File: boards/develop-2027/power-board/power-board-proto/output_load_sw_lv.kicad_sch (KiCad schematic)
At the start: 9 parts, among them Q2 T2N7002BK,LM, Q3 AOD4185

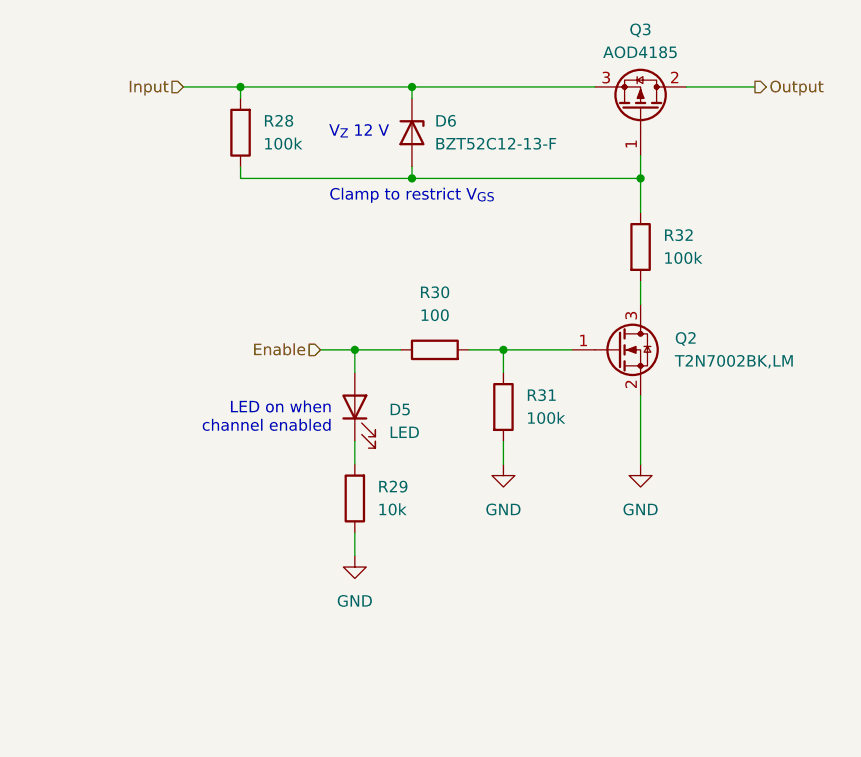
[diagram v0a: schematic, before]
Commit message: add fixes for problems caught by AI design review
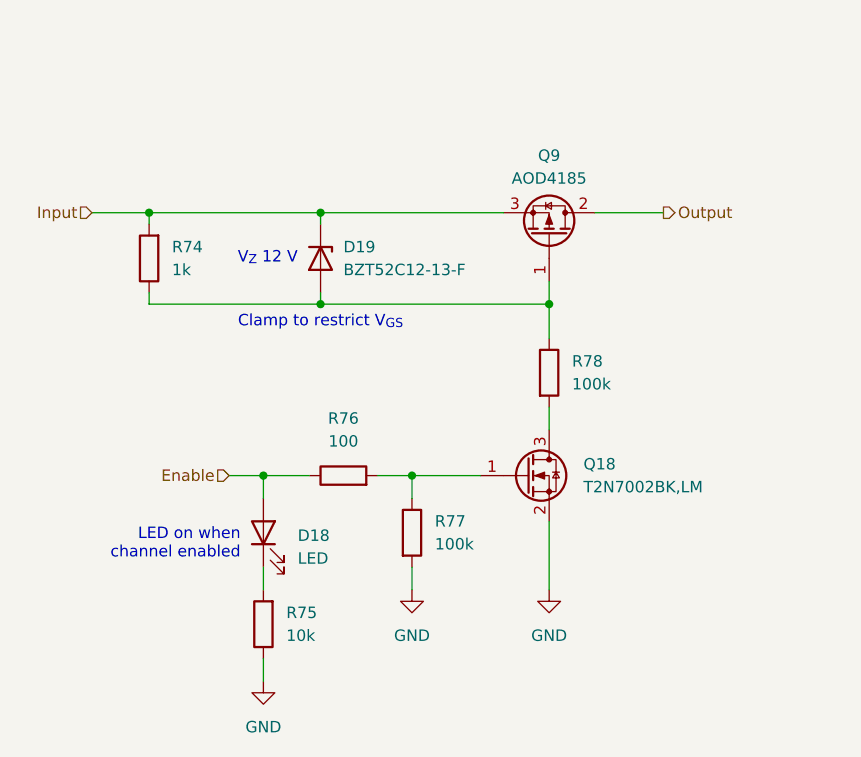
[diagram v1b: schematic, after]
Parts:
- removed D5: LED, LED_SMD:LED_0603_1608Metric_Pad1.05x0.95mm_HandSolder, symbol Device:LED
- removed D6: BZT52C12-13-F, Diode_SMD:D_SOD-123, symbol Device:D_Zener
- removed Q2: T2N7002BK,LM, Package_TO_SOT_SMD:SOT-23-3, symbol Transistor_FET:Q_NMOS_GSD
- removed Q3: AOD4185, Package_TO_SOT_SMD:TO-252-2, symbol Transistor_FET:Q_PMOS_GDS
- removed R28, R31, R32: 100k, Resistor_SMD:R_0603_1608Metric_Pad0.98x0.95mm_HandSolder, symbol Device:R
- removed R29: 10k, Resistor_SMD:R_0603_1608Metric_Pad0.98x0.95mm_HandSolder, symbol Device:R
- removed R30: 100, Resistor_SMD:R_0603_1608Metric_Pad0.98x0.95mm_HandSolder, symbol Device:R
- added D18: LED, LED_SMD:LED_0603_1608Metric_Pad1.05x0.95mm_HandSolder, symbol Device:LED
- added D19: BZT52C12-13-F, Diode_SMD:D_SOD-123, symbol Device:D_Zener
- added Q18: T2N7002BK,LM, Package_TO_SOT_SMD:SOT-23-3, symbol Transistor_FET:Q_NMOS_GSD
- added Q9: AOD4185, Package_TO_SOT_SMD:TO-252-2, symbol Transistor_FET:Q_PMOS_GDS
- added R74: 1k, Resistor_SMD:R_0603_1608Metric_Pad0.98x0.95mm_HandSolder, symbol Device:R
- added R75: 10k, Resistor_SMD:R_0603_1608Metric_Pad0.98x0.95mm_HandSolder, symbol Device:R
- added R76: 100, Resistor_SMD:R_0603_1608Metric_Pad0.98x0.95mm_HandSolder, symbol Device:R
- added R77, R78: 100k, Resistor_SMD:R_0603_1608Metric_Pad0.98x0.95mm_HandSolder, symbol Device:R
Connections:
- net Enable: now also D18.2 (A), R76.1
- net GND: now also Q18.2 (S), R75.1, R77.2
- net Input: now also D19.1 (K), Q9.3 (S), R74.2
- net Output: now also Q9.2 (D)
- new net: Q18.1 (G), R76.2, R77.1
- new net: Q18.3 (D), R78.2
- new net: D18.1 (K), R75.2
- new net: D19.2 (A), Q9.1 (G), R74.1, R78.1
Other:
- title: 40 V, 40 A Output Load Switch -> (none)

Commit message: finalize DigiKey part numbers
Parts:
- D18: Manufacturer P/N (none) -> LTST-C190KRKT; Vendor (none) -> DigiKey; Vendor P/N (none) -> 160-1436-1-ND
- R74: Manufacturer P/N (none) -> RC0603FR-071KL; Vendor (none) -> DigiKey; Vendor P/N (none) -> 311-1.00KHRCT-ND
- R75: Manufacturer P/N (none) -> RC0603FR-0710KL; Vendor (none) -> DigiKey; Vendor P/N (none) -> 311-10.0KHRCT-ND
- R76: Manufacturer P/N (none) -> CRCW0603100RFKEA; Vendor (none) -> DigiKey; Vendor P/N (none) -> 541-100HCT-ND
- R77, R78: Manufacturer P/N (none) -> RC0603FR-07100KL; Vendor (none) -> DigiKey; Vendor P/N (none) -> 311-100KHRCT-ND
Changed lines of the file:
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@@
 			)
 		)
-		(property "Datasheet" ""
+		(property "Datasheet" "https://yageogroup.com/content/datasheet/asset/file/PYU-RC_GROUP_51_ROHS_L"
 			(at 120.65 134.62 0)
 			(hide yes)
@@
 			)
 		)
-		(property "Description" "Resistor"
+		(property "Description" "10 kOhms ±1% 0.1W, 1/10W Chip Resistor 0603 (1608 Metric) Moisture Resistant Thick Film"
 			(at 120.65 134.62 0)
 			(hide yes)
@@
 			)
 		)
-		(property "Manufacturer P/N" ""
+		(property "Manufacturer P/N" "RC0603FR-0710KL"
 			(at 120.65 134.62 0)
 			(hide yes)
@@
 			)
 		)
-		(property "Vendor" ""
+		(property "Vendor" "DigiKey"
 			(at 120.65 134.62 0)
 			(hide yes)
@@
 			)
 		)
-		(property "Vendor P/N" ""
+		(property "Vendor P/N" "311-10.0KHRCT-ND"
 			(at 120.65 134.62 0)
 			(hide yes)
@@
 			)
 		)
-		(property "Datasheet" ""
+		(property "Datasheet" "https://optoelectronics.liteon.com/upload/download/DS-22-99-0151/LTST-C190KRKT.pdf"
 			(at 120.65 124.46 0)
 			(hide yes)
@@
 		(property "Sim.Pins" "1=K 2=A"
 			(at 120.65 124.46 0)
+			(hide yes)
+			(show_name no)
+			(do_not_autoplace no)
+			(effects
+				(font
+					(size 1.27 1.27)
+				)
+			)
+		)
+		(property "Manufacturer P/N" "LTST-C190KRKT"
+			(at 120.65 124.46 90)
+			(hide yes)
+			(show_name no)
+			(do_not_autoplace no)
+			(effects
+				(font
+					(size 1.27 1.27)
+				)
+			)
+		)
+		(property "Vendor" "DigiKey"
+			(at 120.65 124.46 90)
+			(hide yes)
+			(show_name no)
+			(do_not_autoplace no)
+			(effects
+				(font
+					(size 1.27 1.27)
+				)
+			)
+		)
+		(property "Vendor P/N" "160-1436-1-ND "
+			(at 120.65 124.46 90)
 			(hide yes)
 			(show_name no)
@@
 			)
 		)
-		(property "Datasheet" ""
+		(property "Datasheet" "https://yageogroup.com/content/datasheet/asset/file/PYU-RC_GROUP_51_ROHS_L"
 			(at 137.16 124.46 0)
 			(hide yes)
@@
 			)
 		)
-		(property "Description" "Resistor"
+		(property "Description" "100 kOhms ±1% 0.1W, 1/10W Chip Resistor 0603 (1608 Metric) Moisture Resistant Thick Film"
 			(at 137.16 124.46 0)
 			(hide yes)
@@
 			)
 		)
-		(property "Manufacturer P/N" ""
+		(property "Manufacturer P/N" "RC0603FR-07100KL"
 			(at 137.16 124.46 0)
 			(hide yes)
@@
 			)
 		)
-		(property "Vendor" ""
+		(property "Vendor" "DigiKey"
 			(at 137.16 124.46 0)
 			(hide yes)
@@
 			)
 		)
-		(property "Vendor P/N" ""
+		(property "Vendor P/N" "311-100KHRCT-ND"
 			(at 137.16 124.46 0)
 			(hide yes)
@@
 			)
 		)
-		(property "Datasheet" ""
+		(property "Datasheet" "https://www.vishay.com/docs/20035/dcrcwe3.pdf"
 			(at 129.54 118.11 0)
 			(hide yes)
@@
 			)
 		)
-		(property "Description" "Resistor"
+		(property "Description" "100 Ohms ±1% 0.125W, 1/8W Chip Resistor 0603 (1608 Metric) Automotive AEC-Q200 Thick Film"
 			(at 129.54 118.11 0)
 			(hide yes)
@@
 			)
 		)
-		(property "Manufacturer P/N" ""
+		(property "Manufacturer P/N" "CRCW0603100RFKEA"
 			(at 129.54 118.11 0)
 			(hide yes)
@@
 			)
 		)
-		(property "Vendor" ""
+		(property "Vendor" "DigiKey"
 			(at 129.54 118.11 0)
 			(hide yes)
@@
 			)
 		)
-		(property "Vendor P/N" ""
+		(property "Vendor P/N" "541-100HCT-ND"
 			(at 129.54 118.11 0)
 			(hide yes)
@@
 			)
 		)
-		(property "Datasheet" ""
+		(property "Datasheet" "https://yageogroup.com/content/datasheet/asset/file/PYU-RC_GROUP_51_ROHS_L"
 			(at 107.95 93.98 0)
 			(hide yes)
@@
 			)
 		)
-		(property "Description" "Resistor"
+		(property "Description" "1 kOhms ±1% 0.1W, 1/10W Chip Resistor 0603 (1608 Metric) Moisture Resistant Thick Film"
 			(at 107.95 93.98 0)
 			(hide yes)
@@
 			)
 		)
-		(property "Manufacturer P/N" ""
+		(property "Manufacturer P/N" "RC0603FR-071KL"
 			(at 107.95 93.98 0)
 			(hide yes)
@@
 			)
 		)
-		(property "Vendor" ""
+		(property "Vendor" "DigiKey"
 			(at 107.95 93.98 0)
 			(hide yes)
@@
 			)
 		)
-		(property "Vendor P/N" ""
+		(property "Vendor P/N" "311-1.00KHRCT-ND"
 			(at 107.95 93.98 0)
 			(hide yes)
@@
 			)
 		)
-		(property "Datasheet" ""
+		(property "Datasheet" "https://yageogroup.com/content/datasheet/asset/file/PYU-RC_GROUP_51_ROHS_L"
 			(at 152.4 106.68 0)
 			(hide yes)
@@
 			)
 		)
-		(property "Description" "Resistor"
+		(property "Description" "100 kOhms ±1% 0.1W, 1/10W Chip Resistor 0603 (1608 Metric) Moisture Resistant Thick Film"
 			(at 152.4 106.68 0)
 			(hide yes)
@@
 			)
 		)
-		(property "Manufacturer P/N" ""
+		(property "Manufacturer P/N" "RC0603FR-07100KL"
 			(at 152.4 106.68 0)
 			(hide yes)
@@
 			)
 		)
-		(property "Vendor" ""
+		(property "Vendor" "DigiKey"
 			(at 152.4 106.68 0)
 			(hide yes)
@@
 			)
 		)
-		(property "Vendor P/N" ""
+		(property "Vendor P/N" "311-100KHRCT-ND"
 			(at 152.4 106.68 0)
 			(hide yes)
